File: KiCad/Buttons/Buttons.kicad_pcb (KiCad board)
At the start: 2 copper layers, 27.5 x 59.5 mm, 17 parts, among them J1 691137710003, J2 691137710002

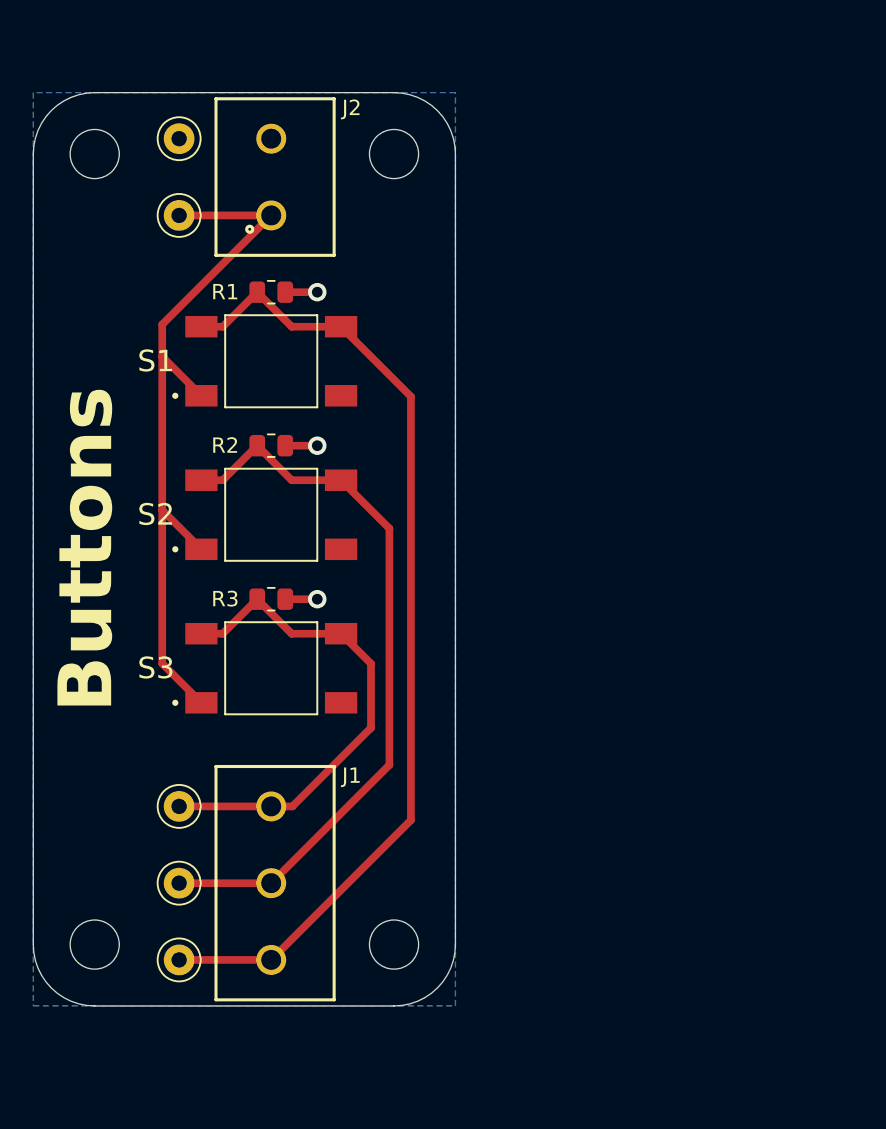
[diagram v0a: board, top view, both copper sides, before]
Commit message: changed buttons pcb layout to be smaller
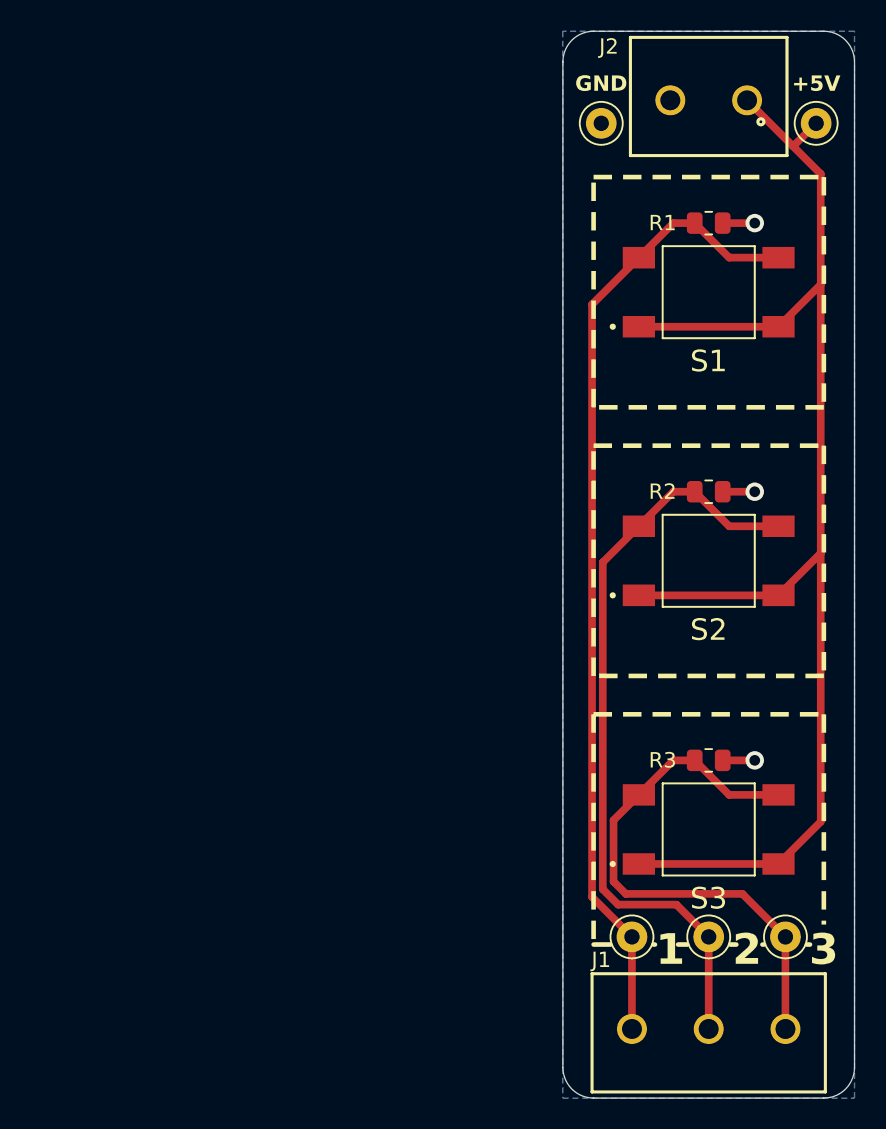
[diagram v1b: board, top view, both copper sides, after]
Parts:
- removed H1, H2, H3, H4: MountingHole, MountingHole:MountingHole_3.2mm_M3
- moved TP1 41.9 mm to (95.5, 63.5), turned to 180 degrees
- moved TP6 40.4 mm to (93.5, 116.5)
- moved TP5 34.7 mm to (88.5, 116.5)
- moved R3 30.4 mm to (88.5, 105.0)
- moved S3 30.4 mm to (88.5, 109.5)
- moved J1 30.0 mm to (88.5, 122.5), turned to 0 degrees
- moved TP4 29.5 mm to (83.5, 116.5)
- moved J2 28.9 mm to (88.5, 62.0), turned to 180 degrees
- moved R1 28.9 mm to (88.5, 70.0)
- moved S1 28.9 mm to (88.5, 74.5)
- moved R2 28.7 mm to (88.5, 87.5)
- moved S2 28.7 mm to (88.5, 92.0)
- moved TP7 27.5 mm to (81.5, 63.5), turned to 180 degrees
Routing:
- net +5V: track 49.0 -> 90.1 mm
- net /Out3: track 32.5 -> 36.0 mm
- net /Out 2: track 47.7 -> 49.8 mm
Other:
- board size 27.5 x 59.5 mm -> 19 x 69.5 mm
- board text added: "+5V"
- board text added: "1"
- board text added: "2"
- board text added: "3"
- board text added: "GND"
- board text removed: "Buttons"
